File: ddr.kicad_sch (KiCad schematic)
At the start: 53 parts, among them U801 MT41K256M16TW

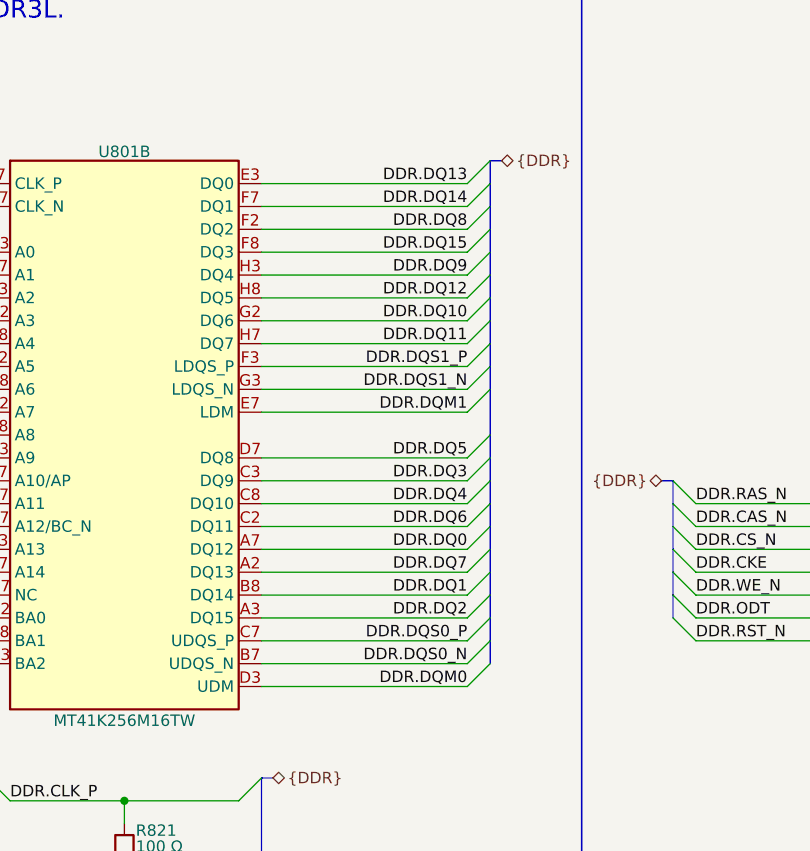
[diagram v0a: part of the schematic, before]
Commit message: Update stackup to 8 layers
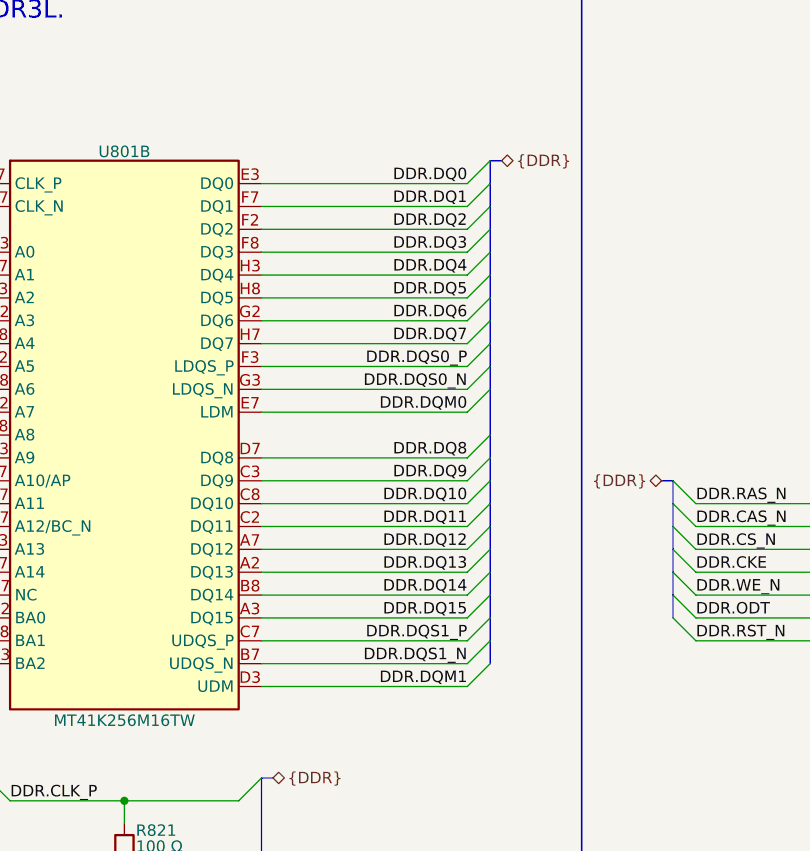
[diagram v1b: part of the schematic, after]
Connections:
- net DDR.DQ0: now also U801.E3 (DQ0); no longer U801.A7 (DQ12)
- net DDR.DQ1: now also U801.F7 (DQ1); no longer U801.B8 (DQ14)
- net DDR.DQ10: now also U801.C8 (DQ10); no longer U801.G2 (DQ6)
- net DDR.DQ11: now also U801.C2 (DQ11); no longer U801.H7 (DQ7)
- net DDR.DQ12: now also U801.A7 (DQ12); no longer U801.H8 (DQ5)
- net DDR.DQ13: now also U801.A2 (DQ13); no longer U801.E3 (DQ0)
- net DDR.DQ14: now also U801.B8 (DQ14); no longer U801.F7 (DQ1)
- net DDR.DQ15: now also U801.A3 (DQ15); no longer U801.F8 (DQ3)
- net DDR.DQ2: now also U801.F2 (DQ2); no longer U801.A3 (DQ15)
- net DDR.DQ3: now also U801.F8 (DQ3); no longer U801.C3 (DQ9)
- net DDR.DQ4: now also U801.H3 (DQ4); no longer U801.C8 (DQ10)
- net DDR.DQ5: now also U801.H8 (DQ5); no longer U801.D7 (DQ8)
- net DDR.DQ6: now also U801.G2 (DQ6); no longer U801.C2 (DQ11)
- net DDR.DQ7: now also U801.H7 (DQ7); no longer U801.A2 (DQ13)
- net DDR.DQ8: now also U801.D7 (DQ8); no longer U801.F2 (DQ2)
- net DDR.DQ9: now also U801.C3 (DQ9); no longer U801.H3 (DQ4)
- net DDR.DQM0: now also U801.E7 (LDM); no longer U801.D3 (UDM)
- net DDR.DQM1: now also U801.D3 (UDM); no longer U801.E7 (LDM)
- net DDR.DQS0_N: now also U801.G3 (LDQS_N); no longer U801.B7 (UDQS_N)
- net DDR.DQS0_P: now also U801.F3 (LDQS_P); no longer U801.C7 (UDQS_P)
- net DDR.DQS1_N: now also U801.B7 (UDQS_N); no longer U801.G3 (LDQS_N)
- net DDR.DQS1_P: now also U801.C7 (UDQS_P); no longer U801.F3 (LDQS_P)
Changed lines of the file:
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@@
 	)
 	(label "DDR.DQ13"
-		(at 292.1 91.44 180)
+		(at 292.1 134.62 180)
 		(effects
 			(font
@@
 	)
 	(label "DDR.DQM1"
-		(at 292.1 116.84 180)
+		(at 292.1 147.32 180)
 		(effects
 			(font
@@
 	)
 	(label "DDR.DQ6"
-		(at 292.1 129.54 180)
+		(at 292.1 106.68 180)
 		(effects
 			(font
@@
 	)
 	(label "DDR.DQS0_N"
-		(at 292.1 144.78 180)
+		(at 292.1 114.3 180)
 		(effects
 			(font
@@
 	)
 	(label "DDR.DQ7"
-		(at 292.1 134.62 180)
+		(at 292.1 109.22 180)
 		(effects
 			(font
@@
 	)
 	(label "DDR.DQ12"
-		(at 292.1 104.14 180)
+		(at 292.1 132.08 180)
 		(effects
 			(font
@@
 	)
 	(label "DDR.DQ14"
-		(at 292.1 93.98 180)
+		(at 292.1 137.16 180)
 		(effects
 			(font
@@
 	)
 	(label "DDR.DQ9"
-		(at 292.1 101.6 180)
+		(at 292.1 124.46 180)
 		(effects
 			(font
@@
 	)
 	(label "DDR.DQM0"
-		(at 292.1 147.32 180)
+		(at 292.1 116.84 180)
 		(effects
 			(font
@@
 	)
 	(label "DDR.DQ1"
-		(at 292.1 137.16 180)
+		(at 292.1 93.98 180)
 		(effects
 			(font
@@
 	)
 	(label "DDR.DQ5"
-		(at 292.1 121.92 180)
+		(at 292.1 104.14 180)
 		(effects
 			(font
@@
 	)
 	(label "DDR.DQS0_P"
-		(at 292.1 142.24 180)
+		(at 292.1 111.76 180)
 		(effects
 			(font
@@
 	)
 	(label "DDR.DQ11"
-		(at 292.1 109.22 180)
+		(at 292.1 129.54 180)
 		(effects
 			(font
@@
 	)
 	(label "DDR.DQ4"
-		(at 292.1 127 180)
+		(at 292.1 101.6 180)
 		(effects
 			(font
@@
 	)
 	(label "DDR.DQ0"
-		(at 292.1 132.08 180)
+		(at 292.1 91.44 180)
 		(effects
 			(font
@@
 	)
 	(label "DDR.DQ10"
-		(at 292.1 106.68 180)
+		(at 292.1 127 180)
 		(effects
 			(font
@@
 	)
 	(label "DDR.DQ2"
-		(at 292.1 139.7 180)
+		(at 292.1 96.52 180)
 		(effects
 			(font
@@
 	)
 	(label "DDR.DQ3"
-		(at 292.1 124.46 180)
+		(at 292.1 99.06 180)
 		(effects
 			(font
@@
 	)
 	(label "DDR.DQ15"
-		(at 292.1 99.06 180)
+		(at 292.1 139.7 180)
 		(effects
 			(font
@@
 	)
 	(label "DDR.DQS1_P"
-		(at 292.1 111.76 180)
+		(at 292.1 142.24 180)
 		(effects
 			(font
@@
 	)
 	(label "DDR.DQS1_N"
-		(at 292.1 114.3 180)
+		(at 292.1 144.78 180)
 		(effects
 			(font
@@
 	)
 	(label "DDR.DQ8"
-		(at 292.1 96.52 180)
+		(at 292.1 121.92 180)
 		(effects
 			(font
@@
 			(justify right bottom)
 		)
-		(property "Netclass" "DDR_L"
+		(property "Netclass" "DDR_U"
 			(at 272.4785 151.13 0)
 			(effects
@@
 			(justify left bottom)
 		)
-		(property "Netclass" "DDR_U"
+		(property "Netclass" "DDR_L"
 			(at 272.4785 87.63 0)
 			(effects

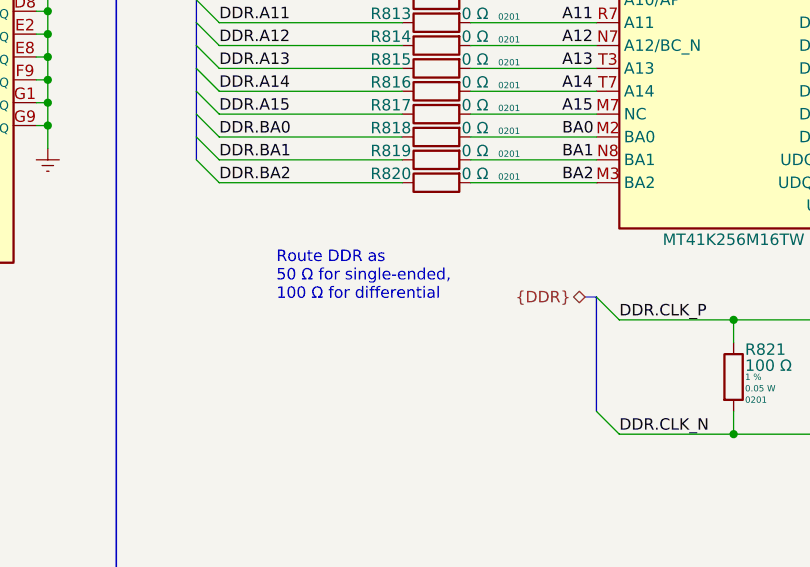
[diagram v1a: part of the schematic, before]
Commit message: Reorganize schematics
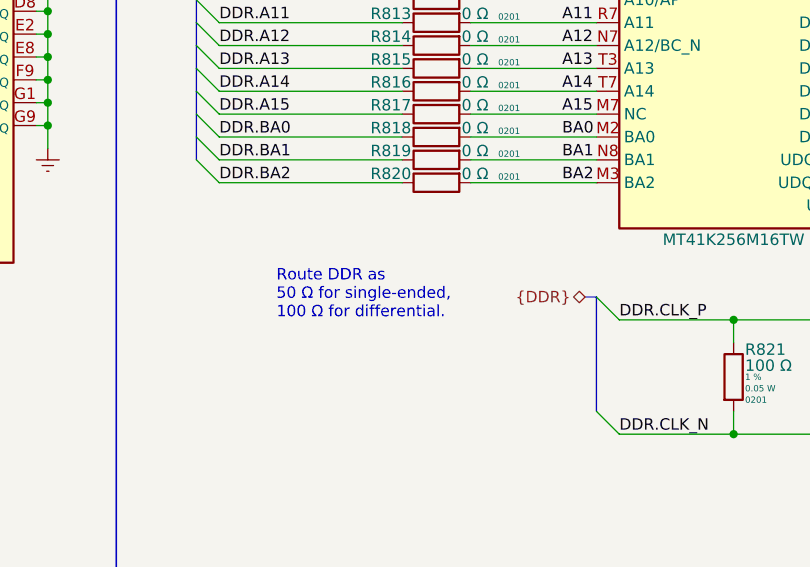
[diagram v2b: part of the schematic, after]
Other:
- note added: "Route DDR as 50 Ω for single-ended, 100 Ω for differential."
- note removed: "Route DDR as 50 Ω for single-ended, 100 Ω for differential"
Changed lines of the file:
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@@
 	(title_block
 		(title "Linux SBC")
-		(date "2026-01-31")
+		(date "2026-02-16")
 		(rev "v1.0.0")
 	)
@@
 		)
 	)
-	(text "Route DDR as\n50 Ω for single-ended,\n100 Ω for differential"
+	(text "Route DDR as\n50 Ω for single-ended,\n100 Ω for differential."
 		(exclude_from_sim no)
-		(at 203.2 152.4 0)
+		(at 203.2 160.02 0)
 		(effects
 			(font
@@
 				(color 194 0 194 1)
 			)
-			(justify left top)
+			(justify left bottom)
 		)
 	)

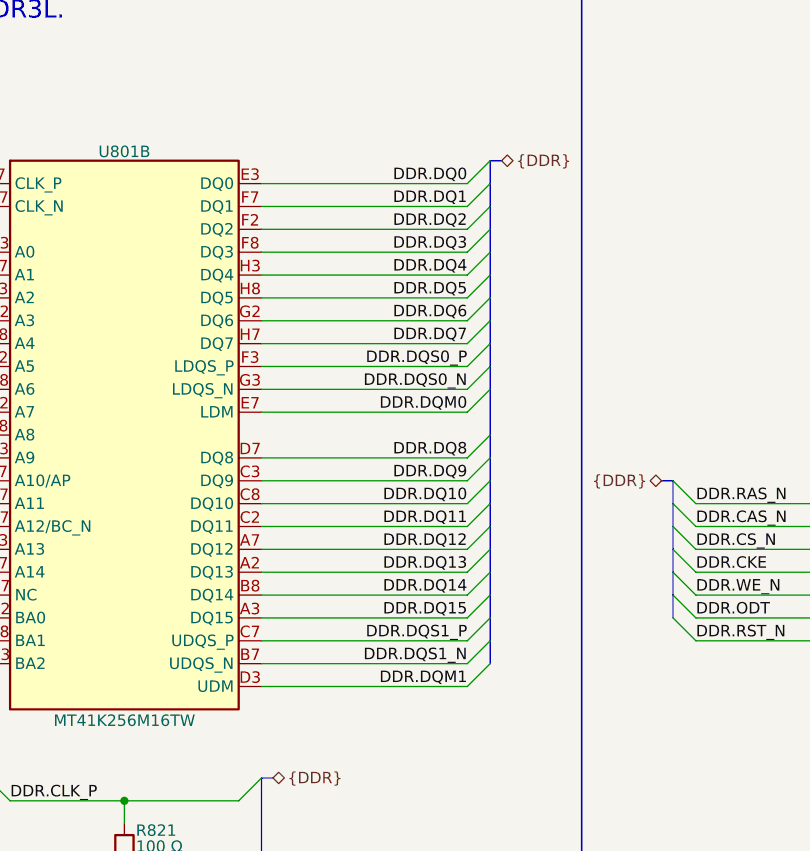
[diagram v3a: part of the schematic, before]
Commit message: DDR: Byte/Bit swap data lines
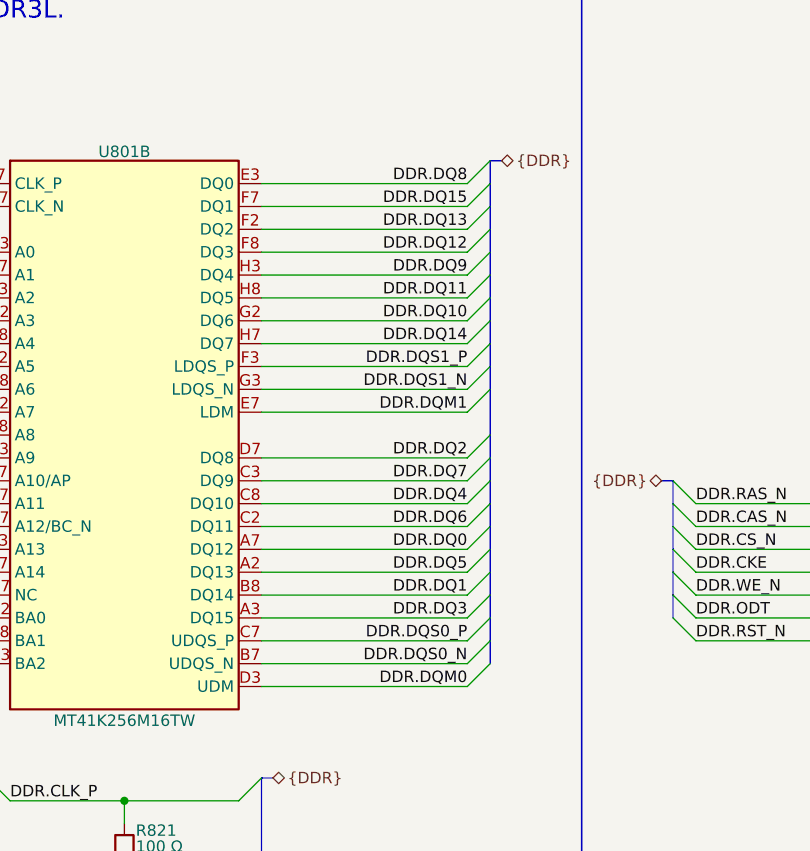
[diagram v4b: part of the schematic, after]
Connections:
- net DDR.DQ0: now also U801.A7 (DQ12); no longer U801.E3 (DQ0)
- net DDR.DQ1: now also U801.B8 (DQ14); no longer U801.F7 (DQ1)
- net DDR.DQ10: now also U801.G2 (DQ6); no longer U801.C8 (DQ10)
- net DDR.DQ11: now also U801.H8 (DQ5); no longer U801.C2 (DQ11)
- net DDR.DQ12: now also U801.F8 (DQ3); no longer U801.A7 (DQ12)
- net DDR.DQ13: now also U801.F2 (DQ2); no longer U801.A2 (DQ13)
- net DDR.DQ14: now also U801.H7 (DQ7); no longer U801.B8 (DQ14)
- net DDR.DQ15: now also U801.F7 (DQ1); no longer U801.A3 (DQ15)
- net DDR.DQ2: now also U801.D7 (DQ8); no longer U801.F2 (DQ2)
- net DDR.DQ3: now also U801.A3 (DQ15); no longer U801.F8 (DQ3)
- net DDR.DQ4: now also U801.C8 (DQ10); no longer U801.H3 (DQ4)
- net DDR.DQ5: now also U801.A2 (DQ13); no longer U801.H8 (DQ5)
- net DDR.DQ6: now also U801.C2 (DQ11); no longer U801.G2 (DQ6)
- net DDR.DQ7: now also U801.C3 (DQ9); no longer U801.H7 (DQ7)
- net DDR.DQ8: now also U801.E3 (DQ0); no longer U801.D7 (DQ8)
- net DDR.DQ9: now also U801.H3 (DQ4); no longer U801.C3 (DQ9)
- net DDR.DQM0: now also U801.D3 (UDM); no longer U801.E7 (LDM)
- net DDR.DQM1: now also U801.E7 (LDM); no longer U801.D3 (UDM)
- net DDR.DQS0_N: now also U801.B7 (UDQS_N); no longer U801.G3 (LDQS_N)
- net DDR.DQS0_P: now also U801.C7 (UDQS_P); no longer U801.F3 (LDQS_P)
- net DDR.DQS1_N: now also U801.G3 (LDQS_N); no longer U801.B7 (UDQS_N)
- net DDR.DQS1_P: now also U801.F3 (LDQS_P); no longer U801.C7 (UDQS_P)
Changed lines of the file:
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@@
 	)
 	(label "DDR.DQ13"
-		(at 292.1 134.62 180)
+		(at 292.1 96.52 180)
 		(effects
 			(font
@@
 	)
 	(label "DDR.DQM1"
-		(at 292.1 147.32 180)
+		(at 292.1 116.84 180)
 		(effects
 			(font
@@
 	)
 	(label "DDR.DQ6"
-		(at 292.1 106.68 180)
+		(at 292.1 129.54 180)
 		(effects
 			(font
@@
 	)
 	(label "DDR.DQS0_N"
-		(at 292.1 114.3 180)
+		(at 292.1 144.78 180)
 		(effects
 			(font
@@
 	)
 	(label "DDR.DQ7"
+		(at 292.1 124.46 180)
+		(effects
+			(font
+				(size 1.27 1.27)
+			)
+			(justify right bottom)
+		)
+	)
+	(label "DDR.DQ12"
+		(at 292.1 99.06 180)
+		(effects
+			(font
+				(size 1.27 1.27)
+			)
+			(justify right bottom)
+		)
+	)
+	(label "DDR.DQ14"
 		(at 292.1 109.22 180)
 		(effects
@@
 		)
 	)
-	(label "DDR.DQ12"
-		(at 292.1 132.08 180)
-		(effects
-			(font
-				(size 1.27 1.27)
-			)
-			(justify right bottom)
-		)
-	)
-	(label "DDR.DQ14"
-		(at 292.1 137.16 180)
-		(effects
-			(font
-				(size 1.27 1.27)
-			)
-			(justify right bottom)
-		)
-	)
 	(label "DDR.DQ9"
-		(at 292.1 124.46 180)
+		(at 292.1 101.6 180)
 		(effects
 			(font
@@
 	)
 	(label "DDR.DQM0"
-		(at 292.1 116.84 180)
+		(at 292.1 147.32 180)
 		(effects
 			(font
@@
 	)
 	(label "DDR.DQ1"
-		(at 292.1 93.98 180)
+		(at 292.1 137.16 180)
 		(effects
 			(font
@@
 	)
 	(label "DDR.DQ5"
-		(at 292.1 104.14 180)
+		(at 292.1 134.62 180)
 		(effects
 			(font
@@
 	)
 	(label "DDR.DQS0_P"
-		(at 292.1 111.76 180)
+		(at 292.1 142.24 180)
 		(effects
 			(font
@@
 	)
 	(label "DDR.DQ11"
-		(at 292.1 129.54 180)
+		(at 292.1 104.14 180)
 		(effects
 			(font
@@
 	)
 	(label "DDR.DQ4"
-		(at 292.1 101.6 180)
+		(at 292.1 127 180)
 		(effects
 			(font
@@
 	)
 	(label "DDR.DQ0"
-		(at 292.1 91.44 180)
+		(at 292.1 132.08 180)
 		(effects
 			(font
@@
 	)
 	(label "DDR.DQ10"
-		(at 292.1 127 180)
+		(at 292.1 106.68 180)
 		(effects
 			(font
@@
 	)
 	(label "DDR.DQ2"
-		(at 292.1 96.52 180)
+		(at 292.1 121.92 180)
 		(effects
 			(font
@@
 	)
 	(label "DDR.DQ3"
-		(at 292.1 99.06 180)
+		(at 292.1 139.7 180)
 		(effects
 			(font
@@
 	)
 	(label "DDR.DQ15"
-		(at 292.1 139.7 180)
+		(at 292.1 93.98 180)
 		(effects
 			(font
@@
 	)
 	(label "DDR.DQS1_P"
-		(at 292.1 142.24 180)
+		(at 292.1 111.76 180)
 		(effects
 			(font
@@
 	)
 	(label "DDR.DQS1_N"
-		(at 292.1 144.78 180)
+		(at 292.1 114.3 180)
 		(effects
 			(font
@@
 	)
 	(label "DDR.DQ8"
-		(at 292.1 121.92 180)
-		(effects
-			(font
+		(at 292.1 91.44 180)
+		(effects
+			(font

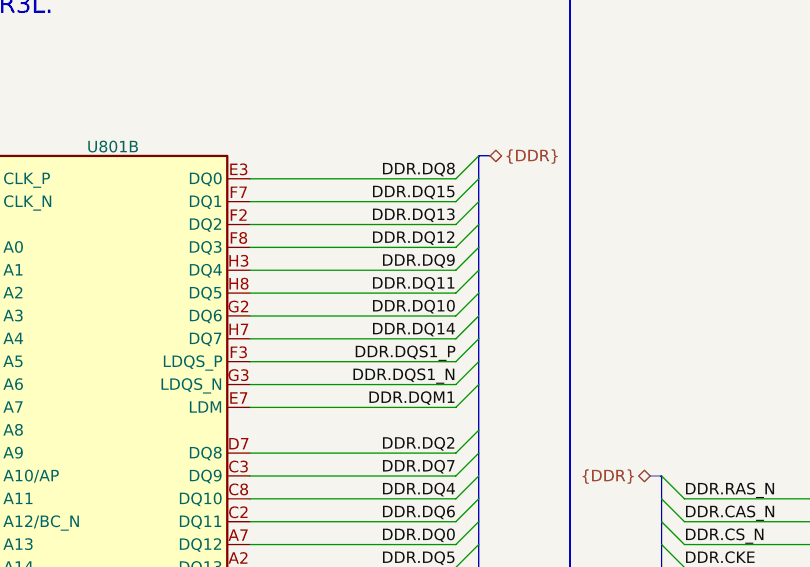
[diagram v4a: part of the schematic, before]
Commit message: Switch to a 8-layer stackup
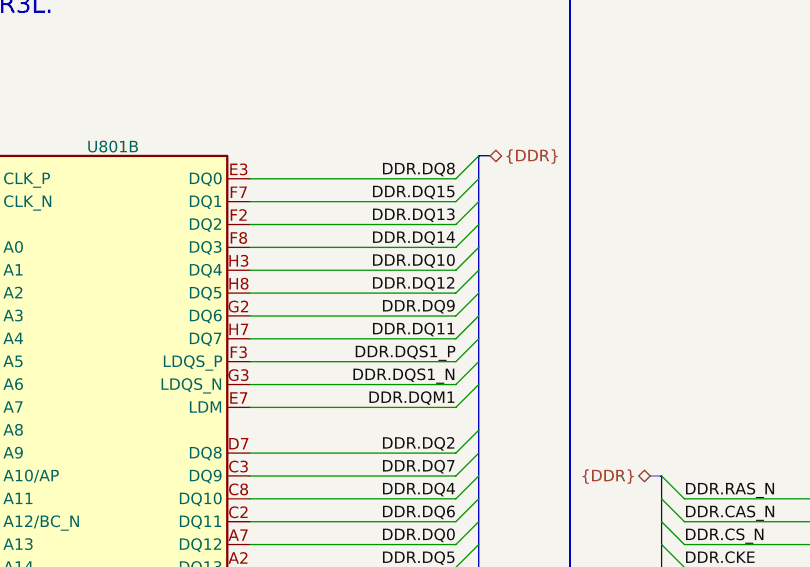
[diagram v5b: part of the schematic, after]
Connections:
- net DDR.DQ10: now also U801.H3 (DQ4); no longer U801.G2 (DQ6)
- net DDR.DQ11: now also U801.H7 (DQ7); no longer U801.H8 (DQ5)
- net DDR.DQ12: now also U801.H8 (DQ5); no longer U801.F8 (DQ3)
- net DDR.DQ14: now also U801.F8 (DQ3); no longer U801.H7 (DQ7)
- net DDR.DQ9: now also U801.G2 (DQ6); no longer U801.H3 (DQ4)
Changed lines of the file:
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@@
 	)
 	(label "DDR.DQ12"
+		(at 292.1 104.14 180)
+		(effects
+			(font
+				(size 1.27 1.27)
+			)
+			(justify right bottom)
+		)
+	)
+	(label "DDR.DQ14"
 		(at 292.1 99.06 180)
 		(effects
@@
 		)
 	)
-	(label "DDR.DQ14"
-		(at 292.1 109.22 180)
-		(effects
-			(font
-				(size 1.27 1.27)
-			)
-			(justify right bottom)
-		)
-	)
 	(label "DDR.DQ9"
-		(at 292.1 101.6 180)
+		(at 292.1 106.68 180)
 		(effects
 			(font
@@
 	)
 	(label "DDR.DQ11"
-		(at 292.1 104.14 180)
+		(at 292.1 109.22 180)
 		(effects
 			(font
@@
 	)
 	(label "DDR.DQ10"
-		(at 292.1 106.68 180)
-		(effects
-			(font
+		(at 292.1 101.6 180)
+		(effects
+			(font
